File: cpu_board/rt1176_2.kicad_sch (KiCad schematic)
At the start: 14 parts, among them U2 MIMXRT1176

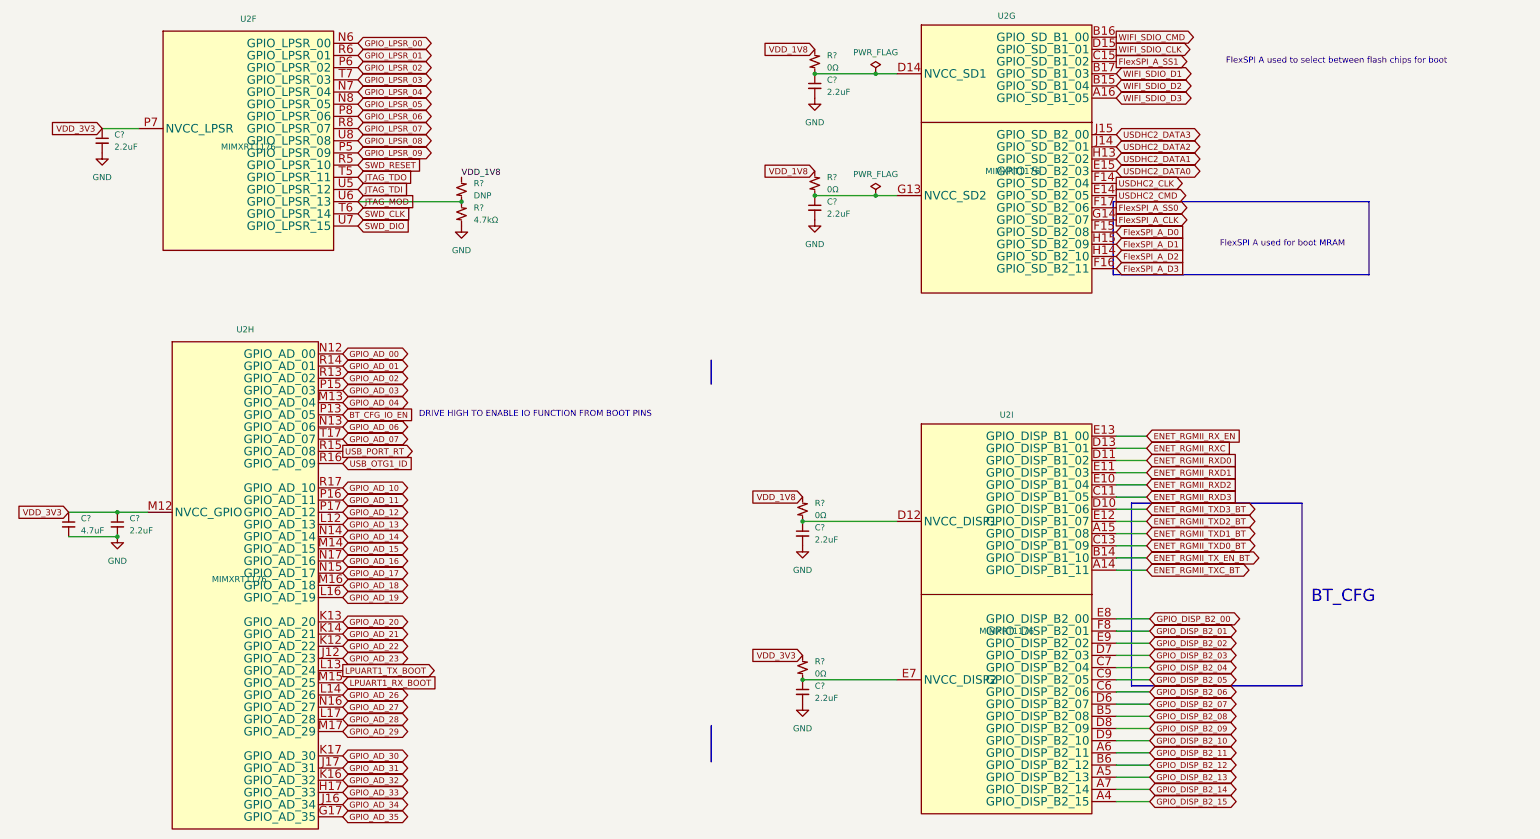
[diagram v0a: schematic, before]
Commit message: clean up board2board connector and organize TODOs
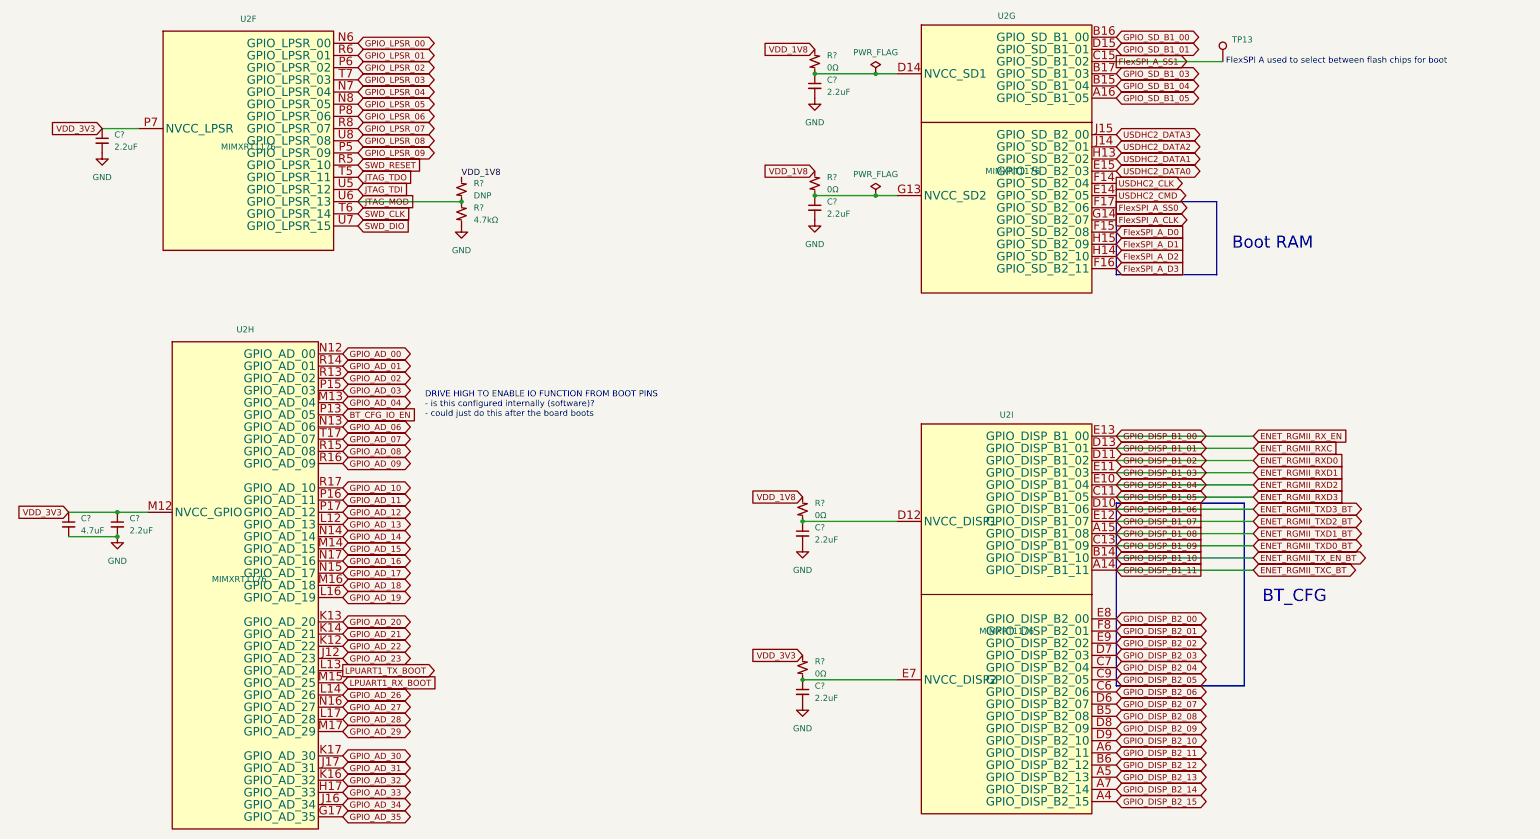
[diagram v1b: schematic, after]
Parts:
- added TP13: TestPoint, TestPoint:TestPoint_Pad_1.5x1.5mm, symbol Connector:TestPoint
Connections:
- net FlexSPI_A_SS1: now also TP13.1
- net USB_OTG1_ID renamed GPIO_AD_09
- net USB_PORT_RT renamed GPIO_AD_08
- net WIFI_SDIO_CLK renamed GPIO_SD_B1_01
- net WIFI_SDIO_CMD renamed GPIO_SD_B1_00
- net WIFI_SDIO_D1 renamed GPIO_SD_B1_03
- net WIFI_SDIO_D2 renamed GPIO_SD_B1_04
- net WIFI_SDIO_D3 renamed GPIO_SD_B1_05
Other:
- note added: "Boot RAM"
- note added: "DRIVE HIGH TO ENABLE IO FUNCTION FROM BOOT PINS - is this configured internally (software)? - could just do this after the board boots"
- note removed: "DRIVE HIGH TO ENABLE IO FUNCTION FROM BOOT PINS"
- note removed: "FlexSPI A used for boot MRAM"

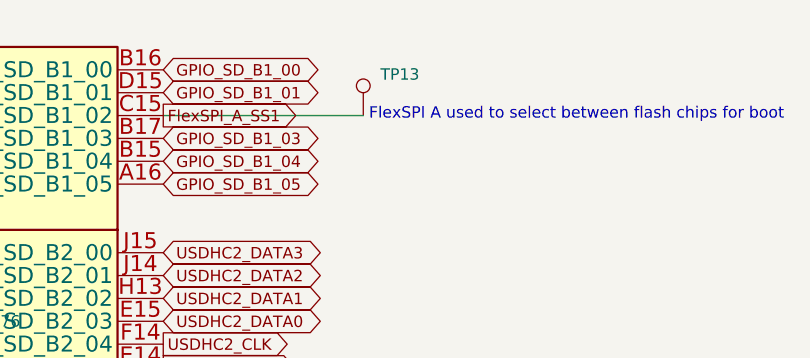
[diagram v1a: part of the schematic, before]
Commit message: route most of power distribution
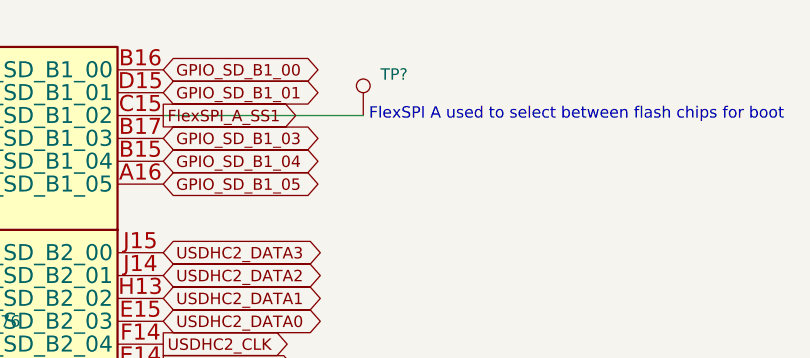
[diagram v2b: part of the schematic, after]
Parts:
- TP?: renamed from TP13; footprint TestPoint:TestPoint_Pad_1.5x1.5mm -> TestPoint:TestPoint_Pad_1.0x1.0mm; JLCPCB P/N (none) -> C221678
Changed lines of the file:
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@@
         )
         (path "/c4fd7bdd-408e-44be-b66f-e6a18a0ca6e3/41b8ad77-fc22-40ff-9aa2-f9a432177b3d"
-          (reference "C45") (unit 1)
+          (reference "C44") (unit 1)
         )
       )
@@
         )
         (path "/c4fd7bdd-408e-44be-b66f-e6a18a0ca6e3/41b8ad77-fc22-40ff-9aa2-f9a432177b3d"
-          (reference "C44") (unit 1)
+          (reference "C45") (unit 1)
         )
       )
@@
   (symbol (lib_id "Connector:TestPoint") (at 302.895 74.295 0) (unit 1)
     (in_bom yes) (on_board yes) (dnp no)
-    (property "Reference" "TP13" (at 304.8 69.723 0)
+    (property "Reference" "TP?" (at 304.8 69.723 0)
       (effects (font (size 1.27 1.27)) (justify left))
     )
@@
       (effects (font (size 1.27 1.27)) (justify left) hide)
     )
-    (property "Footprint" "TestPoint:TestPoint_Pad_1.5x1.5mm" (at 307.975 74.295 0)
+    (property "Footprint" "TestPoint:TestPoint_Pad_1.0x1.0mm" (at 307.975 74.295 0)
       (effects (font (size 1.27 1.27)) hide)
     )
@@
       (effects (font (size 1.27 1.27)) hide)
     )
-    (property "JLCPCB P/N" "" (at 302.895 74.295 0)
+    (property "JLCPCB P/N" "C221678" (at 302.895 74.295 0)
       (effects (font (size 1.27 1.27)) hide)
     )
@@
       (project "cpu_board"
         (path "/c4fd7bdd-408e-44be-b66f-e6a18a0ca6e3/0a33bd80-4856-46ea-ab2b-780eb050e9ec"
-          (reference "TP13") (unit 1)
+          (reference "TP?") (unit 1)
         )
         (path "/c4fd7bdd-408e-44be-b66f-e6a18a0ca6e3/ff5944eb-9859-4dab-aeb3-20c6124220de"
-          (reference "TP17") (unit 1)
-        )
-        (path "/c4fd7bdd-408e-44be-b66f-e6a18a0ca6e3/41b8ad77-fc22-40ff-9aa2-f9a432177b3d"
-          (reference "TP18") (unit 1)
+          (reference "TP?") (unit 1)
+        )
+        (path "/c4fd7bdd-408e-44be-b66f-e6a18a0ca6e3/41b8ad77-fc22-40ff-9aa2-f9a432177b3d"
+          (reference "TP3") (unit 1)
         )
       )
@@
   (symbol (lib_id "power:GND") (at 215.265 208.28 0) (unit 1)
     (in_bom yes) (on_board yes) (dnp no) (fields_autoplaced)
-    (property "Reference" "#PWR038" (at 215.265 214.63 0)
+    (property "Reference" "#PWR039" (at 215.265 214.63 0)
       (effects (font (size 1.27 1.27)) hide)
     )
@@
       (project "cpu_board"
         (path "/c4fd7bdd-408e-44be-b66f-e6a18a0ca6e3/41b8ad77-fc22-40ff-9aa2-f9a432177b3d"
-          (reference "#PWR038") (unit 1)
+          (reference "#PWR039") (unit 1)
         )
       )
@@
         )
         (path "/c4fd7bdd-408e-44be-b66f-e6a18a0ca6e3/41b8ad77-fc22-40ff-9aa2-f9a432177b3d"
-          (reference "R14") (unit 1)
+          (reference "R9") (unit 1)
         )
       )
@@
         )
         (path "/c4fd7bdd-408e-44be-b66f-e6a18a0ca6e3/41b8ad77-fc22-40ff-9aa2-f9a432177b3d"
-          (reference "R19") (unit 1)
+          (reference "R14") (unit 1)
         )
       )
@@
         )
         (path "/c4fd7bdd-408e-44be-b66f-e6a18a0ca6e3/41b8ad77-fc22-40ff-9aa2-f9a432177b3d"
-          (reference "R16") (unit 1)
+          (reference "R11") (unit 1)
         )
       )
@@
         )
         (path "/c4fd7bdd-408e-44be-b66f-e6a18a0ca6e3/41b8ad77-fc22-40ff-9aa2-f9a432177b3d"
-          (reference "R18") (unit 1)
+          (reference "R13") (unit 1)
         )
       )
@@
   (symbol (lib_id "power:GND") (at 69.215 93.345 0) (unit 1)
     (in_bom yes) (on_board yes) (dnp no) (fields_autoplaced)
-    (property "Reference" "#PWR034" (at 69.215 99.695 0)
+    (property "Reference" "#PWR035" (at 69.215 99.695 0)
       (effects (font (size 1.27 1.27)) hide)
     )
@@
       (project "cpu_board"
         (path "/c4fd7bdd-408e-44be-b66f-e6a18a0ca6e3/41b8ad77-fc22-40ff-9aa2-f9a432177b3d"
-          (reference "#PWR034") (unit 1)
+          (reference "#PWR035") (unit 1)
         )
       )
@@
         )
         (path "/c4fd7bdd-408e-44be-b66f-e6a18a0ca6e3/41b8ad77-fc22-40ff-9aa2-f9a432177b3d"
-          (reference "R17") (unit 1)
+          (reference "R12") (unit 1)
         )
       )
@@
         )
         (path "/c4fd7bdd-408e-44be-b66f-e6a18a0ca6e3/41b8ad77-fc22-40ff-9aa2-f9a432177b3d"
-          (reference "R15") (unit 1)
+          (reference "R10") (unit 1)
         )
       )
@@
   (symbol (lib_id "power:GND") (at 217.805 81.915 0) (unit 1)
     (in_bom yes) (on_board yes) (dnp no) (fields_autoplaced)
-    (property "Reference" "#PWR039" (at 217.805 88.265 0)
+    (property "Reference" "#PWR040" (at 217.805 88.265 0)
       (effects (font (size 1.27 1.27)) hide)
     )
@@
       (project "cpu_board"
         (path "/c4fd7bdd-408e-44be-b66f-e6a18a0ca6e3/41b8ad77-fc22-40ff-9aa2-f9a432177b3d"
-          (reference "#PWR039") (unit 1)
+          (reference "#PWR040") (unit 1)
         )
       )
@@
   (symbol (lib_id "power:GND") (at 215.265 175.26 0) (unit 1)
     (in_bom yes) (on_board yes) (dnp no) (fields_autoplaced)
-    (property "Reference" "#PWR037" (at 215.265 181.61 0)
+    (property "Reference" "#PWR038" (at 215.265 181.61 0)
       (effects (font (size 1.27 1.27)) hide)
     )
@@
       (project "cpu_board"
         (path "/c4fd7bdd-408e-44be-b66f-e6a18a0ca6e3/41b8ad77-fc22-40ff-9aa2-f9a432177b3d"
-          (reference "#PWR037") (unit 1)
+          (reference "#PWR038") (unit 1)
         )
       )
@@
   (symbol (lib_id "power:GND") (at 144.145 108.585 0) (unit 1)
     (in_bom yes) (on_board yes) (dnp no) (fields_autoplaced)
-    (property "Reference" "#PWR036" (at 144.145 114.935 0)
+    (property "Reference" "#PWR037" (at 144.145 114.935 0)
       (effects (font (size 1.27 1.27)) hide)
     )
@@
       (project "cpu_board"
         (path "/c4fd7bdd-408e-44be-b66f-e6a18a0ca6e3/41b8ad77-fc22-40ff-9aa2-f9a432177b3d"
-          (reference "#PWR036") (unit 1)
+          (reference "#PWR037") (unit 1)
         )
       )
@@
   (symbol (lib_id "power:GND") (at 217.805 107.315 0) (unit 1)
     (in_bom yes) (on_board yes) (dnp no) (fields_autoplaced)
-    (property "Reference" "#PWR040" (at 217.805 113.665 0)
+    (property "Reference" "#PWR041" (at 217.805 113.665 0)
       (effects (font (size 1.27 1.27)) hide)
     )
@@
       (project "cpu_board"
         (path "/c4fd7bdd-408e-44be-b66f-e6a18a0ca6e3/41b8ad77-fc22-40ff-9aa2-f9a432177b3d"
-          (reference "#PWR040") (unit 1)
+          (reference "#PWR041") (unit 1)
         )
       )
@@
   (symbol (lib_id "power:GND") (at 72.39 173.355 0) (unit 1)
     (in_bom yes) (on_board yes) (dnp no) (fields_autoplaced)
-    (property "Reference" "#PWR035" (at 72.39 179.705 0)
+    (property "Reference" "#PWR036" (at 72.39 179.705 0)
       (effects (font (size 1.27 1.27)) hide)
     )
@@
       (project "cpu_board"
         (path "/c4fd7bdd-408e-44be-b66f-e6a18a0ca6e3/41b8ad77-fc22-40ff-9aa2-f9a432177b3d"
-          (reference "#PWR035") (unit 1)
-        )
-      )
+          (reference "#PWR036") (unit 1)
+        )
+      )

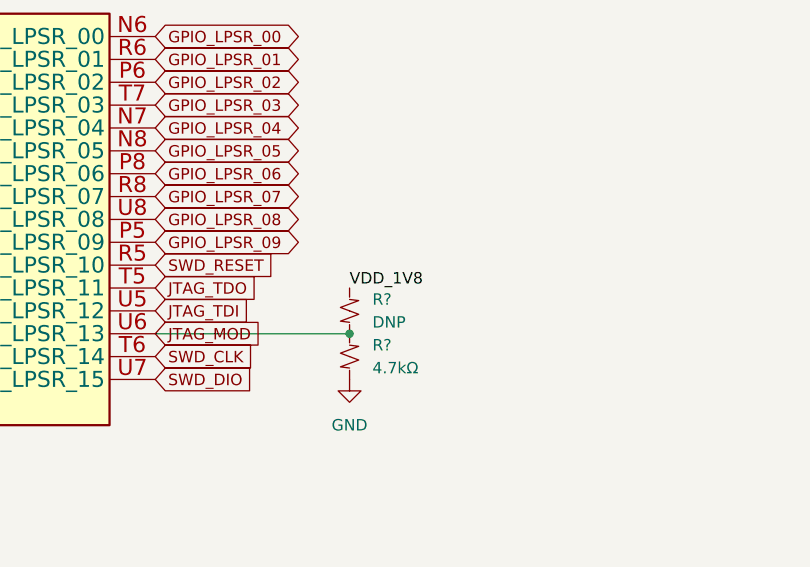
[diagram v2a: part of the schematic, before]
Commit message: clean up pwr slightly
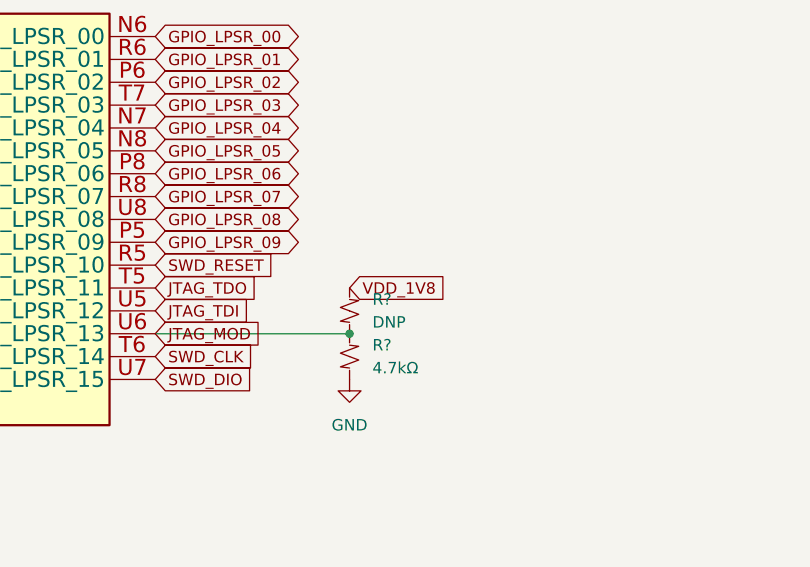
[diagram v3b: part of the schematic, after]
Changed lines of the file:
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@@
     (effects (font (size 2.54 2.54)) (justify left bottom))
-  )
-  (label "VDD_1V8" (at 144.145 98.425 0) (fields_autoplaced)
-    (effects (font (size 1.27 1.27)) (justify left bottom))
   )
   (global_label "GPIO_DISP_B1_11" (shape input) (at 280.67 180.34 0) (fields_autoplaced)
@@
       (effects (font (size 1.27 1.27)) (justify left) hide)
     )
+  )
+  (global_label "VDD_1V8" (shape input) (at 144.145 98.425 0) (fields_autoplaced)
+    (effects (font (size 1.27 1.27)) (justify left))
+    (property "Intersheetrefs" "${INTERSHEET_REFS}" (at 155.234 98.425 0)
+      (effects (font (size 1.27 1.27)) (justify left) hide)
+    )

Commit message: floorplan complete
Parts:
- removed R?: DNP, Resistor_SMD:R_0402_1005Metric, symbol Device:R_Small_US
- removed R? (x4): 0Ω, Resistor_SMD:R_0402_1005Metric, symbol Device:R_Small_US
- removed TP?: TestPoint, TestPoint:TestPoint_Pad_1.0x1.0mm, symbol Connector:TestPoint
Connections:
- net VDD_1V8: now also C?.1, C?.1, C?.1, U2.D12 (NVCC_DISP1), U2.D14 (NVCC_SD1), U2.G13 (NVCC_SD2)
- net VDD_3V3: now also C?.1, U2.E7 (NVCC_DISP2)

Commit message: add models and power diagram
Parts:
- U2: footprint adcs:BGA289C80P17X17_1400X14000X152 -> adcs:U_MIMXRT1176DVMAA_NXP
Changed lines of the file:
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@@
       (effects (font (size 1.27 1.27)))
     )
-    (property "Footprint" "adcs:BGA289C80P17X17_1400X14000X152" (at 97.79 182.245 0)
+    (property "Footprint" "adcs:U_MIMXRT1176DVMAA_NXP" (at 97.79 182.245 0)
       (effects (font (size 1.27 1.27)) hide)
     )
@@
     (property "Footprint (for JLCPCB)" "" (at 97.79 180.975 0)
       (effects (font (size 1.27 1.27)) hide)
+    )
+    (property "DigiKey Part Number" "" (at 97.79 180.975 0)
+      (effects (font (size 1.27 1.27)) hide)
+    )
+    (property "Tolerance" "" (at 97.79 180.975 0)
+      (effects (font (size 1.27 1.27)))
+    )
+    (property "Power Rating" "" (at 97.79 180.975 0)
+      (effects (font (size 1.27 1.27)))
     )
     (pin "L9")
@@
       (effects (font (size 1.27 1.27)))
     )
-    (property "Footprint" "adcs:BGA289C80P17X17_1400X14000X152" (at 99.695 92.075 0)
+    (property "Footprint" "adcs:U_MIMXRT1176DVMAA_NXP" (at 99.695 92.075 0)
       (effects (font (size 1.27 1.27)) hide)
     )
@@
     (property "Footprint (for JLCPCB)" "" (at 99.695 90.805 0)
       (effects (font (size 1.27 1.27)) hide)
+    )
+    (property "DigiKey Part Number" "" (at 99.695 90.805 0)
+      (effects (font (size 1.27 1.27)) hide)
+    )
+    (property "Tolerance" "" (at 99.695 90.805 0)
+      (effects (font (size 1.27 1.27)))
+    )
+    (property "Power Rating" "" (at 99.695 90.805 0)
+      (effects (font (size 1.27 1.27)))
     )
     (pin "L9")
@@
       (effects (font (size 1.27 1.27)))
     )
-    (property "Footprint" "adcs:BGA289C80P17X17_1400X14000X152" (at 257.81 193.04 0)
+    (property "Footprint" "adcs:U_MIMXRT1176DVMAA_NXP" (at 257.81 193.04 0)
       (effects (font (size 1.27 1.27)) hide)
     )
@@
     (property "Footprint (for JLCPCB)" "" (at 257.81 191.77 0)
       (effects (font (size 1.27 1.27)) hide)
+    )
+    (property "DigiKey Part Number" "" (at 257.81 191.77 0)
+      (effects (font (size 1.27 1.27)) hide)
+    )
+    (property "Tolerance" "" (at 257.81 191.77 0)
+      (effects (font (size 1.27 1.27)))
+    )
+    (property "Power Rating" "" (at 257.81 191.77 0)
+      (effects (font (size 1.27 1.27)))
     )
     (pin "L9")
@@
       (effects (font (size 1.27 1.27)))
     )
-    (property "Footprint" "adcs:BGA289C80P17X17_1400X14000X152" (at 259.08 97.155 0)
+    (property "Footprint" "adcs:U_MIMXRT1176DVMAA_NXP" (at 259.08 97.155 0)
       (effects (font (size 1.27 1.27)) hide)
     )
@@
       (effects (font (size 1.27 1.27)) hide)
     )
+    (property "DigiKey Part Number" "" (at 259.08 95.885 0)
+      (effects (font (size 1.27 1.27)) hide)
+    )
+    (property "Tolerance" "" (at 259.08 95.885 0)
+      (effects (font (size 1.27 1.27)))
+    )
+    (property "Power Rating" "" (at 259.08 95.885 0)
+      (effects (font (size 1.27 1.27)))
+    )
     (pin "L9")

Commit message: continue work on fanout
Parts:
- C? (x7): footprint Capacitor_SMD:C_0402_1005Metric -> adcs:Perfect_0201
- R?: footprint Resistor_SMD:R_0402_1005Metric -> adcs:Perfect_0402
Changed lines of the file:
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@@
       (effects (font (size 1.27 1.27)) (justify left))
     )
-    (property "Footprint" "Capacitor_SMD:C_0402_1005Metric" (at 217.805 79.375 0)
+    (property "Footprint" "adcs:Perfect_0201" (at 217.805 79.375 0)
       (effects (font (size 1.27 1.27)) hide)
     )
@@
       (effects (font (size 1.27 1.27)) (justify left))
     )
-    (property "Footprint" "Capacitor_SMD:C_0402_1005Metric" (at 217.805 104.775 0)
+    (property "Footprint" "adcs:Perfect_0201" (at 217.805 104.775 0)
       (effects (font (size 1.27 1.27)) hide)
     )
@@
       (effects (font (size 1.27 1.27)) (justify left))
     )
-    (property "Footprint" "Capacitor_SMD:C_0402_1005Metric" (at 62.23 170.815 0)
+    (property "Footprint" "adcs:Perfect_0201" (at 62.23 170.815 0)
       (effects (font (size 1.27 1.27)) hide)
     )
@@
     (property "Footprint (for JLCPCB)" "0402" (at 62.23 170.815 0)
       (effects (font (size 1.27 1.27)) hide)
+    )
+    (property "DigiKey Part Number" "" (at 62.23 170.815 0)
+      (effects (font (size 1.27 1.27)) hide)
+    )
+    (property "Tolerance" "" (at 62.23 170.815 0)
+      (effects (font (size 1.27 1.27)))
+    )
+    (property "Power Rating" "" (at 62.23 170.815 0)
+      (effects (font (size 1.27 1.27)))
     )
     (pin "1")
@@
       (effects (font (size 1.27 1.27)) (justify left))
     )
-    (property "Footprint" "Capacitor_SMD:C_0402_1005Metric" (at 69.215 90.805 0)
+    (property "Footprint" "adcs:Perfect_0201" (at 69.215 90.805 0)
       (effects (font (size 1.27 1.27)) hide)
     )
@@
       (effects (font (size 1.27 1.27)) (justify left))
     )
-    (property "Footprint" "Capacitor_SMD:C_0402_1005Metric" (at 72.39 170.815 0)
+    (property "Footprint" "adcs:Perfect_0201" (at 72.39 170.815 0)
       (effects (font (size 1.27 1.27)) hide)
     )
@@
       (effects (font (size 1.27 1.27)) (justify right))
     )
-    (property "Footprint" "Resistor_SMD:R_0402_1005Metric" (at 144.145 106.045 0)
+    (property "Footprint" "adcs:Perfect_0402" (at 144.145 106.045 0)
       (effects (font (size 1.27 1.27)) hide)
     )
@@
       (effects (font (size 1.27 1.27)) (justify left))
     )
-    (property "Footprint" "Capacitor_SMD:C_0402_1005Metric" (at 215.265 172.72 0)
+    (property "Footprint" "adcs:Perfect_0201" (at 215.265 172.72 0)
       (effects (font (size 1.27 1.27)) hide)
     )
@@
       (effects (font (size 1.27 1.27)) (justify left))
     )
-    (property "Footprint" "Capacitor_SMD:C_0402_1005Metric" (at 215.265 205.74 0)
-      (effects (font (size 1.27 1.27)) hide)
-    )
+    (property "Footprint" "adcs:Perfect_0201" (at 215.265 205.74 0)
+      (effects (font (size 1.27 1.27)) hide)
+    )
